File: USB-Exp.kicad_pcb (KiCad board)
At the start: 2 copper layers, 55 x 35 mm, 34 parts, among them J1 USB_B_Micro, J2 Barrel_Jack, J3 USB-A-S-X-X-SM2-R, J4 USB-A-S-X-X-SM2-R, J5 USB-A-S-X-X-SM2-R, J6 ICSP, J7 FTDI, P1 MYSX_2.6, Q1 Q_NMOS_GSD, Q2 Q_NMOS_GSD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

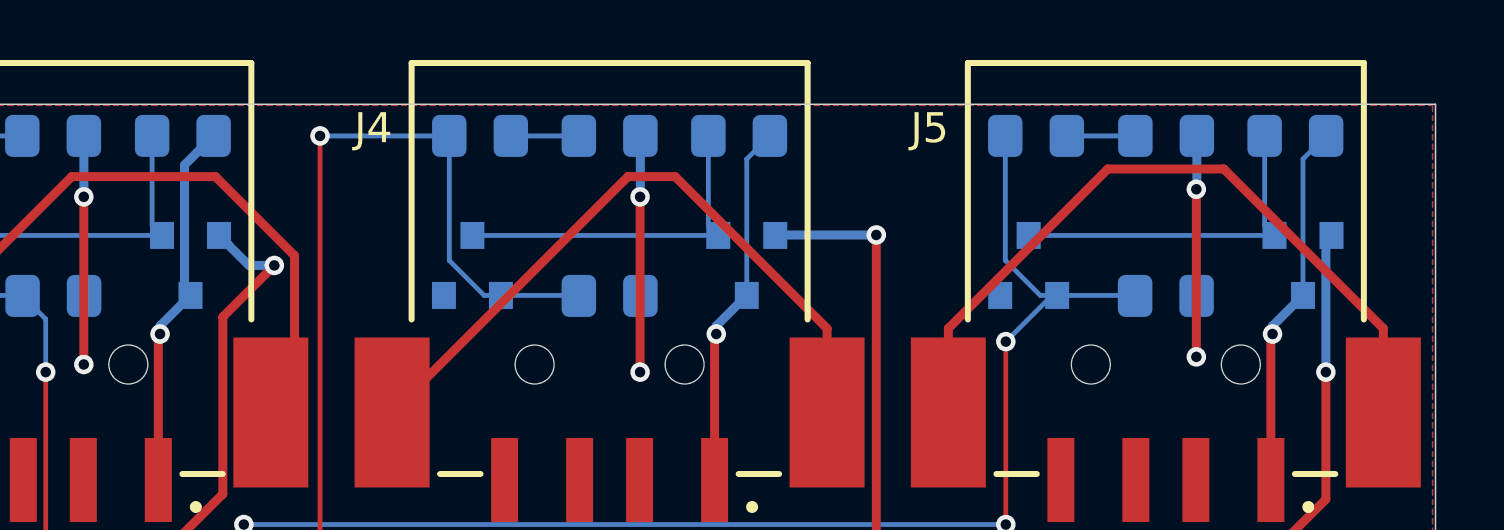
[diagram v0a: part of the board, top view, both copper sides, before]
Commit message: fixed R, R8 and R9 connection
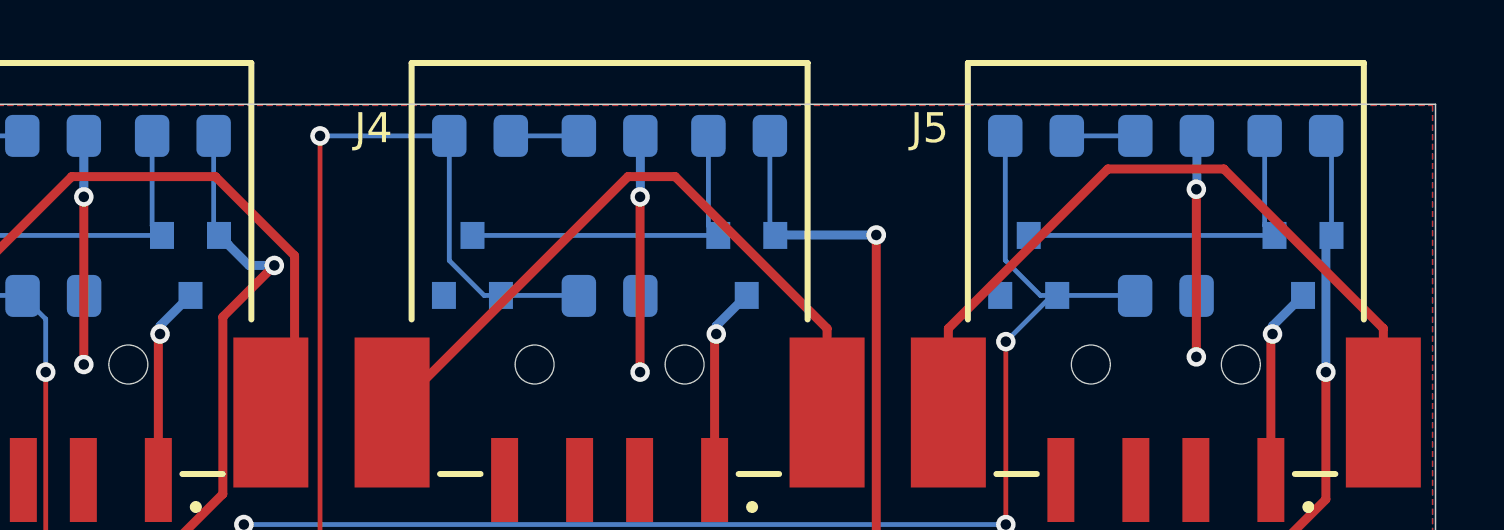
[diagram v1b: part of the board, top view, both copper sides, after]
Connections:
- R7 pad 1: Net-(J3-Pad01) -> Vin
- R8 pad 1: Net-(J4-Pad01) -> Vin
- R9 pad 1: Net-(J5-Pad01) -> Vin
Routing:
- net Vin: track 136.5 -> 146.7 mm
- net Net-(J5-Pad01): track 12.3 -> 6.68 mm
- net Net-(J4-Pad01): track 12.2 -> 6.60 mm
- net Net-(J3-Pad01): track 12.4 -> 6.88 mm
